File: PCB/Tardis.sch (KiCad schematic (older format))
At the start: 50 parts, among them Q1 2N3904, U1 RDC2072S12, U2 L4940, U3 MT8888C, U4 MT8888C, Y1 3.579545MHz, Y2 3.579545MHz

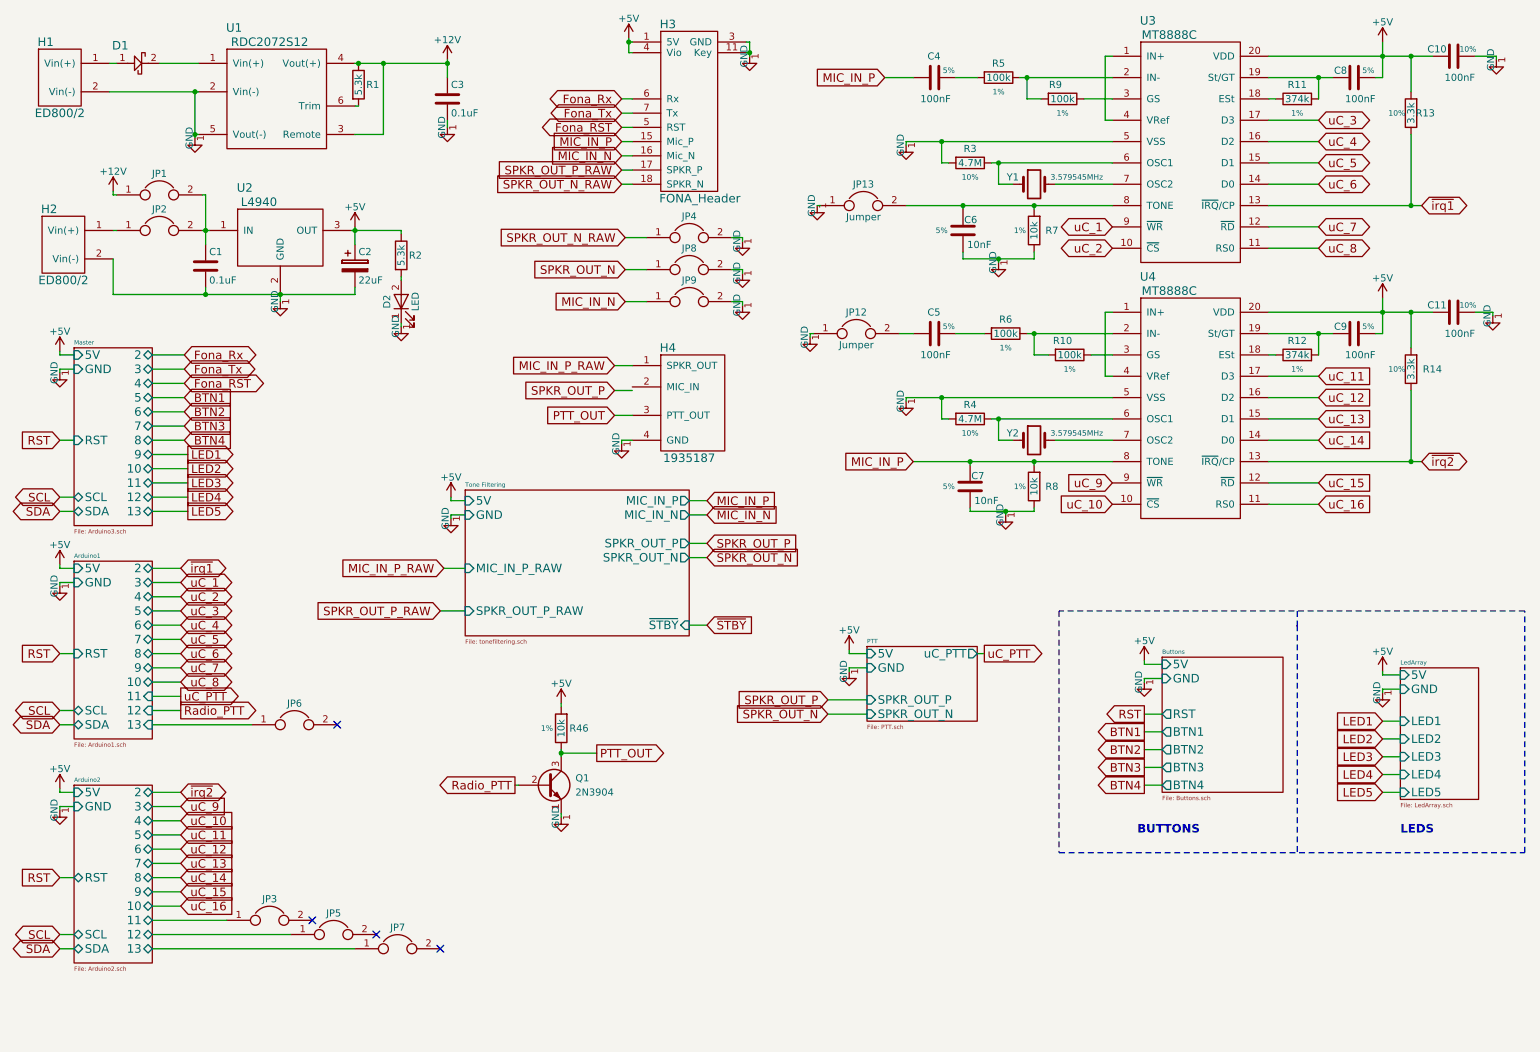
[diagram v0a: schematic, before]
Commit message: Added jumpers to bypass amp
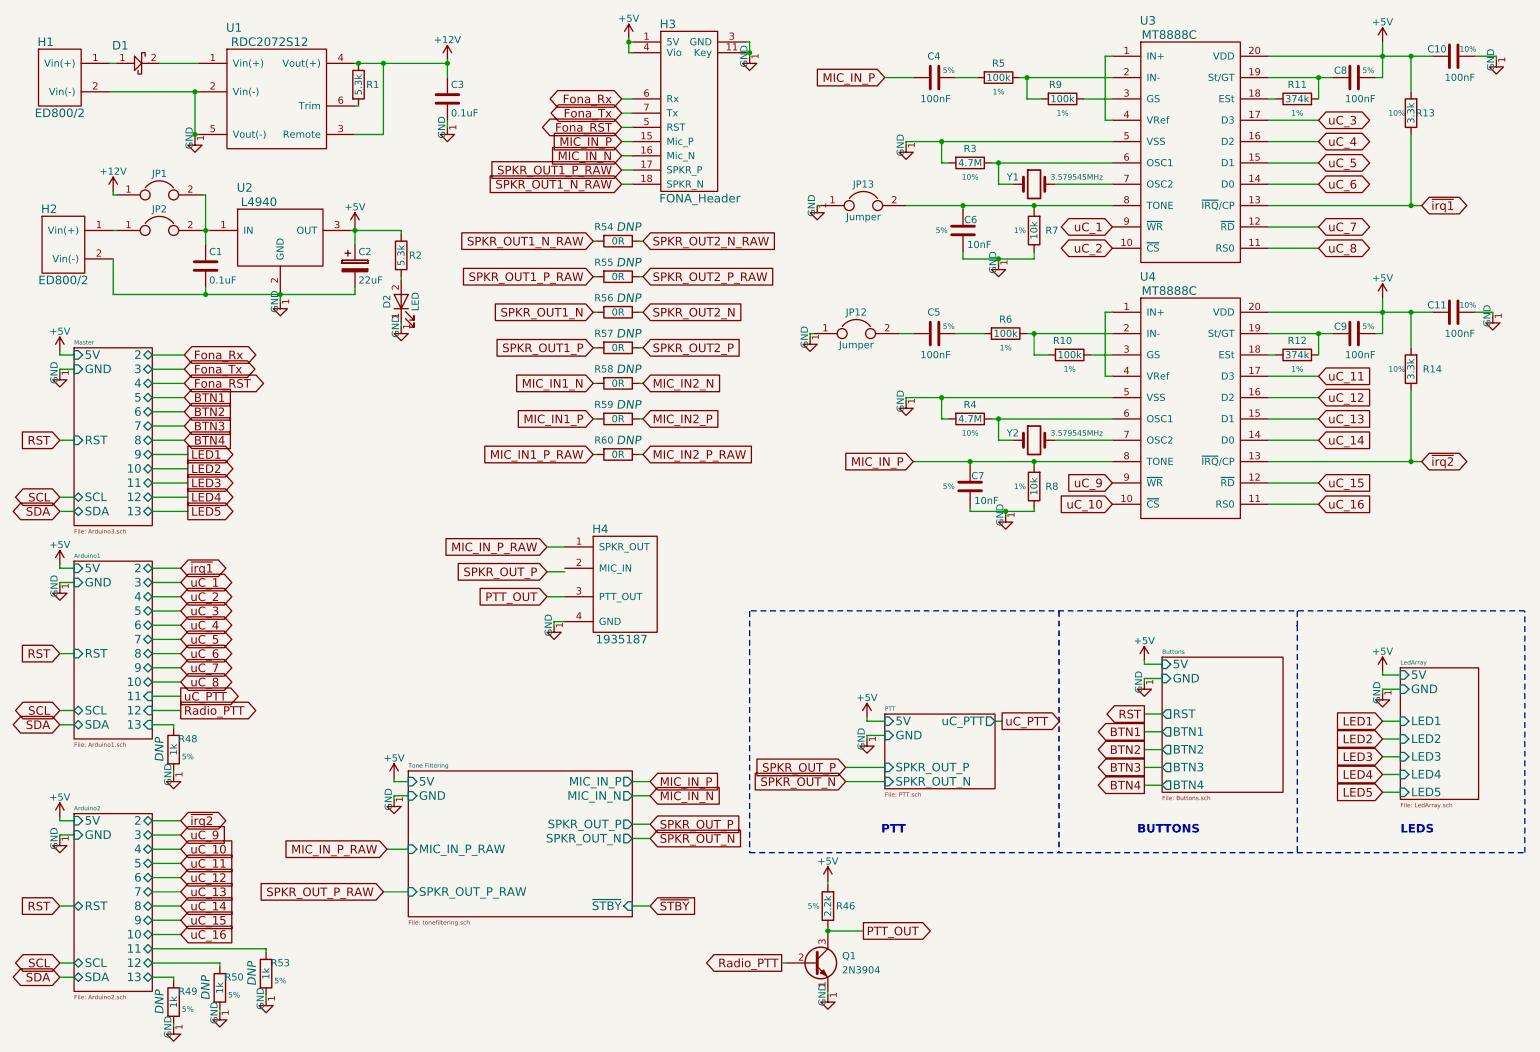
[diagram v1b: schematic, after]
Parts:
- removed JP3, JP4, JP5, JP6, JP7, JP8, JP9: Jumper, symbol Jumper
- added R48, R49, R50, R53: 1k, symbol R
- added R54, R55, R56, R57, R58, R59, R60: 0R, symbol R
- R46: value 10k -> 2.2k; % 1% -> 5%
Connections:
- net Arduino1/13: now also R48.1
- net Arduino2/11: now also R53.1
- net Arduino2/12: now also R50.1
- net Arduino2/13: now also R49.1
- net SPKR_OUT_P_RAW: no longer H3.17 (SPKR_P)
- net SPKR_OUT_N_RAW renamed SPKR_OUT1_N_RAW
- net SPKR_OUT1_N_RAW: now also R54.2
- new net MIC_IN1_N: R58.2
- new net MIC_IN1_P: R59.2
- new net MIC_IN1_P_RAW: R60.2
- new net MIC_IN2_N: R58.1
- new net MIC_IN2_P: R59.1
- new net MIC_IN2_P_RAW: R60.1
- new net SPKR_OUT1_N: R56.2
- new net SPKR_OUT1_P: R57.2
- new net SPKR_OUT1_P_RAW: H3.17 (SPKR_P), R55.2
- new net SPKR_OUT2_N: R56.1
- new net SPKR_OUT2_N_RAW: R54.1
- new net SPKR_OUT2_P: R57.1
- new net SPKR_OUT2_P_RAW: R55.1
- no-connect marks 4 -> 0
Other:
- note added: "PTT"
- moved on the sheet: H4, Q1, R46

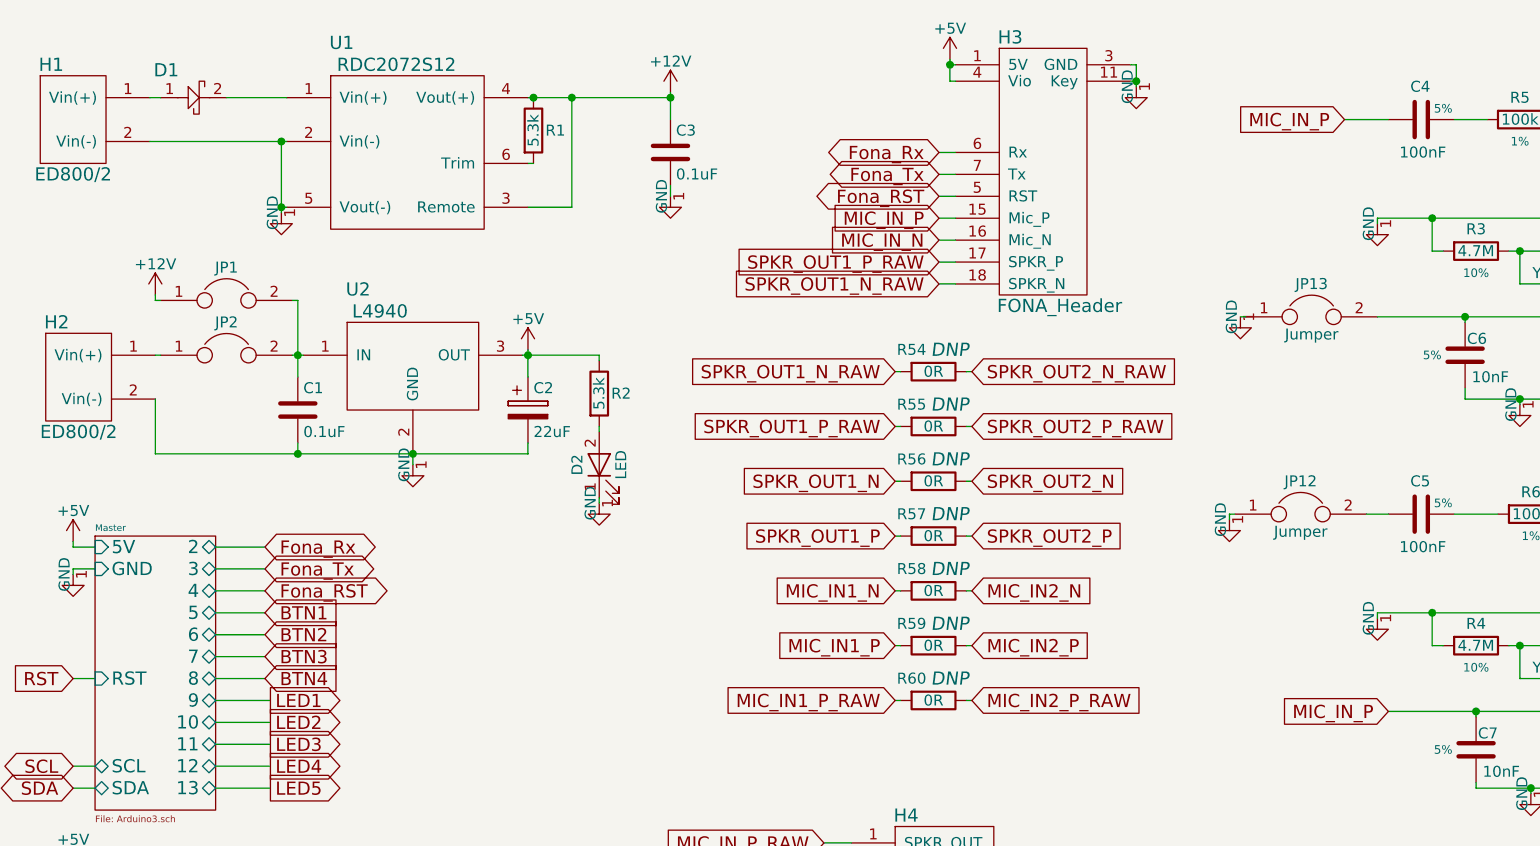
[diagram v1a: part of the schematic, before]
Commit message: Adding footprints
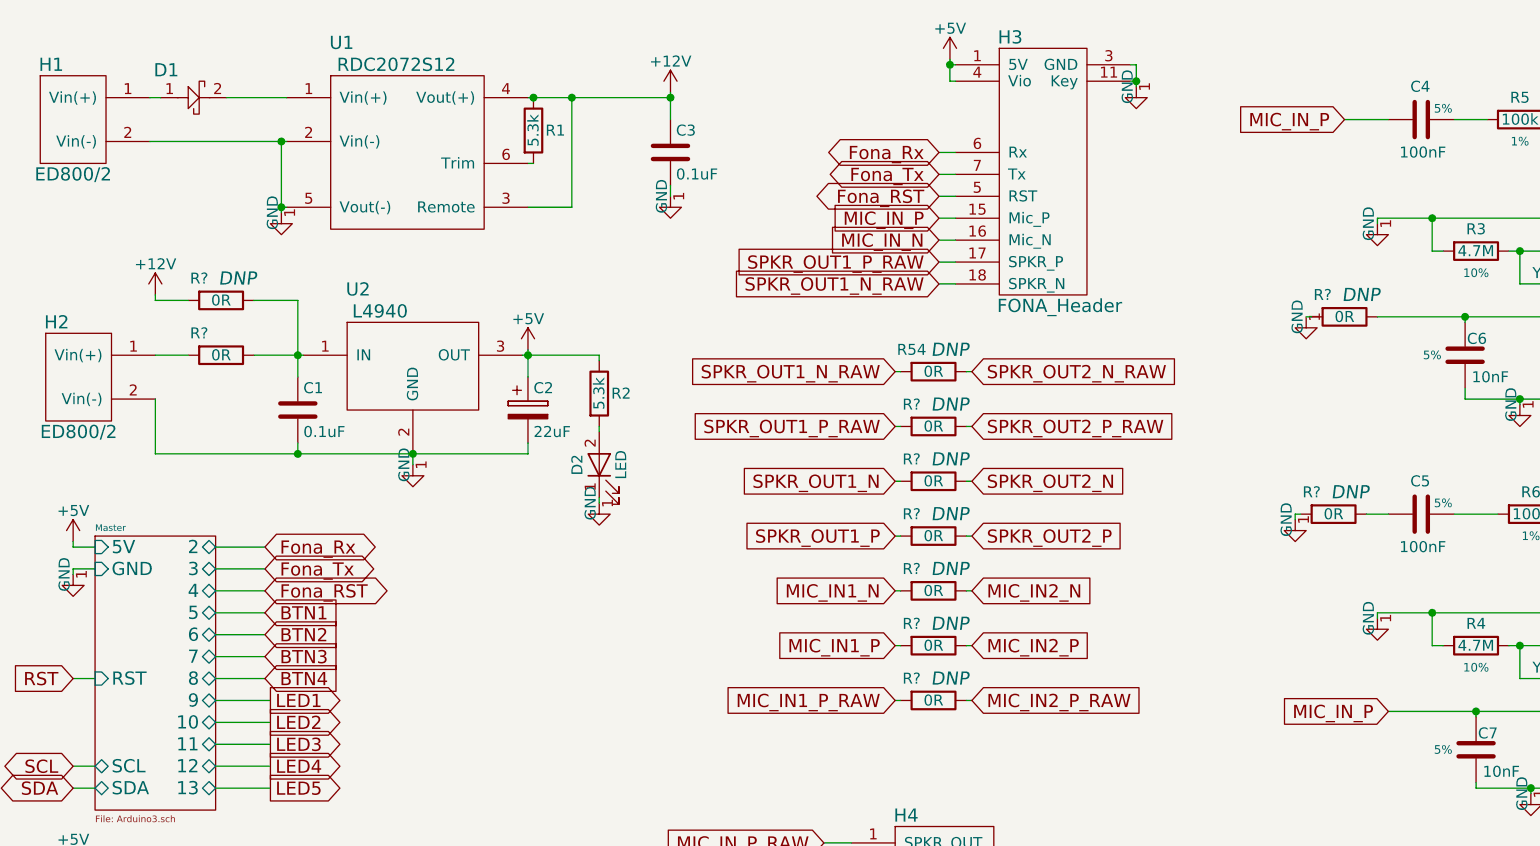
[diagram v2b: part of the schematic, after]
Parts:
- removed JP1, JP12, JP13, JP2: Jumper, symbol Jumper
- removed R55, R56, R57, R58, R59, R60: 0R, symbol R
- added R? (x10): 0R, Resistor_THT:R_Axial_DIN0207_L6.3mm_D2.5mm_P2.54mm_Vertical, symbol R
- H3: footprint (none) -> Pin_Headers:Pin_Header_Straight_1x18_Pitch2.54mm
- H4: footprint (none) -> Footprints:1935187
- R54: footprint (none) -> Resistor_THT:R_Axial_DIN0207_L6.3mm_D2.5mm_P2.54mm_Vertical; % 5% -> Jumper; Digikey (none) -> A105988CT-ND
- U2: footprint Footprints:L4940_dpak -> TO_SOT_Packages_THT:TO-220-3_Vertical
- U3, U4: footprint Footprints:20-3518-10 -> Footprints:SOIC-20
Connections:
- net +12V: now also R?.2
- net MIC_IN1_N: now also R?.2
- net MIC_IN1_P: now also R?.2
- net MIC_IN1_P_RAW: now also R?.2
- net MIC_IN2_N: now also R?.1
- net MIC_IN2_P: now also R?.1
- net MIC_IN2_P_RAW: now also R?.1
- net SPKR_OUT1_N: now also R?.2
- net SPKR_OUT1_P: now also R?.2
- net SPKR_OUT1_P_RAW: now also R?.2
- net SPKR_OUT2_N: now also R?.1
- net SPKR_OUT2_P: now also R?.1
- net SPKR_OUT2_P_RAW: now also R?.1
- net at H2.1 (Vin(+)): now also R?.2
- net at C1.1, U2.1 (IN): now also R?.1, R?.1
- net at C6.2, R7.2, U3.8 (TONE): now also R?.1
- net at C5.2: now also R?.1

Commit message: Adding footprints cont.
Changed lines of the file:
@@
 	3250 2075 3250 2100
 Wire Wire Line
-	3125 900  3125 1400
+	3125 1400 3125 900
 Connection ~ 3125 900
 $Comp
